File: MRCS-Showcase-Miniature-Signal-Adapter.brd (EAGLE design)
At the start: 24.5 x 24.5 mm, 19 parts

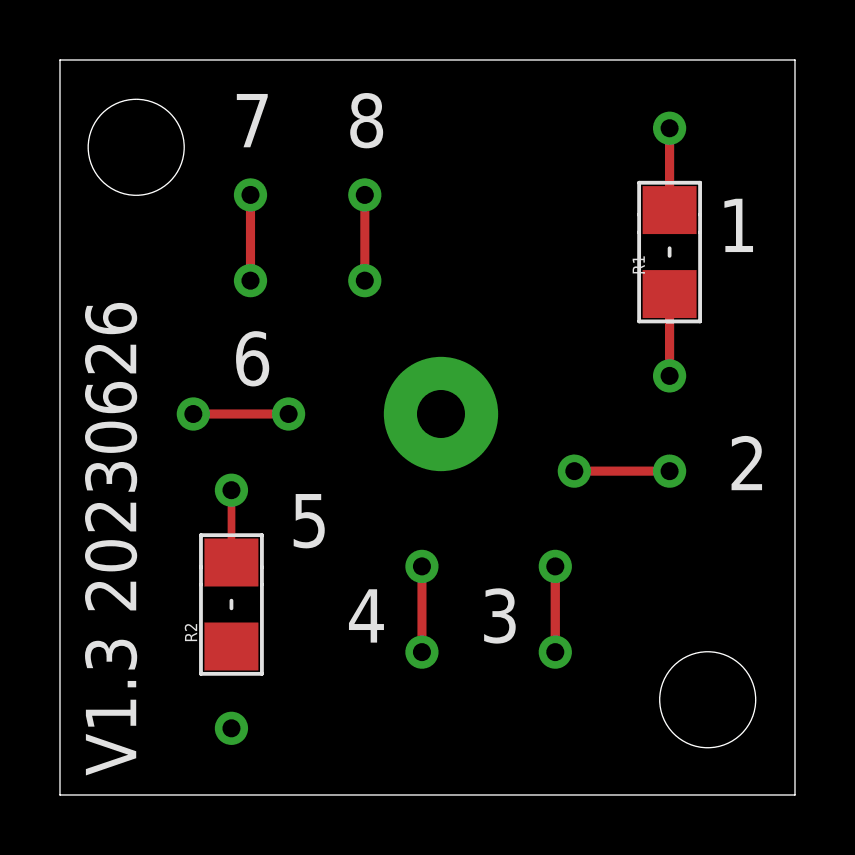
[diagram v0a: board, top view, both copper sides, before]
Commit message: First production version
Showcase miniature signal base for 1 or 2 head signal, requested by Allison Dendy
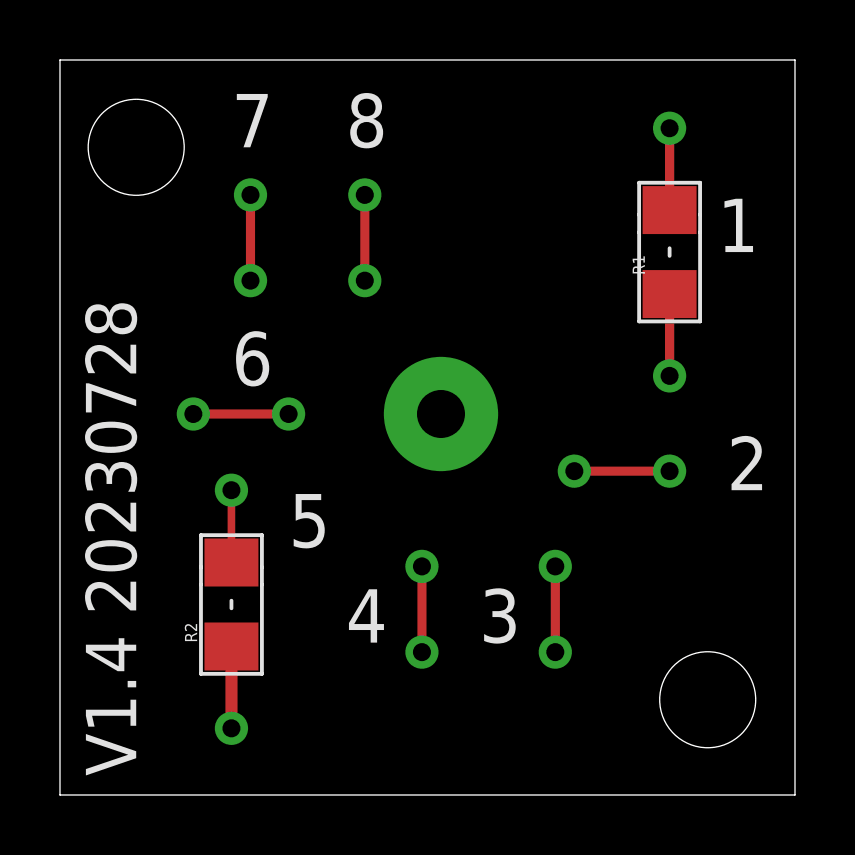
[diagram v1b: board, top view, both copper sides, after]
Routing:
- net N$3: track 0.00 -> 2.73 mm
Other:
- board text added: "R1"
- board text added: "R2"
- board text added: "V1.4 20230728"
- board text removed: "V1.3 20230626"
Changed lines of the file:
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@@
 <layer number="98" name="Guide" color="6" fill="1" visible="no" active="no"/>
 <layer number="99" name="Anatomie" color="7" fill="1" visible="no" active="no"/>
-<layer number="100" name="Muster" color="7" fill="1" visible="no" active="no"/>
-<layer number="101" name="Hidden" color="57" fill="4" visible="yes" active="yes"/>
-<layer number="102" name="Changes" color="13" fill="1" visible="yes" active="yes"/>
-<layer number="103" name="tMap" color="29" fill="4" visible="no" active="yes"/>
-<layer number="104" name="Name" color="16" fill="1" visible="yes" active="yes"/>
-<layer number="105" name="tPlate" color="7" fill="1" visible="no" active="yes"/>
-<layer number="106" name="bPlate" color="7" fill="1" visible="no" active="yes"/>
-<layer number="107" name="Crop" color="7" fill="1" visible="no" active="yes"/>
-<layer number="108" name="fp8" color="7" fill="1" visible="no" active="yes"/>
-<layer number="109" name="fp9" color="7" fill="1" visible="no" active="yes"/>
-<layer number="110" name="fp0" color="7" fill="1" visible="no" active="yes"/>
-<layer number="111" name="bdokum" color="7" fill="1" visible="no" active="yes"/>
-<layer number="112" name="tSilk" color="7" fill="1" visible="no" active="no"/>
-<layer number="113" name="IDFDebug" color="7" fill="1" visible="no" active="yes"/>
-<layer number="114" name="Rect_Pads" color="7" fill="1" visible="no" active="yes"/>
-<layer number="115" name="_tsilk" color="7" fill="1" visible="no" active="yes"/>
-<layer number="116" name="Patch_BOT" color="9" fill="4" visible="no" active="yes"/>
-<layer number="117" name="tTestmark" color="7" fill="1" visible="no" active="yes"/>
-<layer number="118" name="Rect_Pads" color="7" fill="1" visible="no" active="no"/>
-<layer number="119" name="_tNames" color="7" fill="1" visible="no" active="yes"/>
-<layer number="120" name="_bNames" color="7" fill="1" visible="no" active="yes"/>
-<layer number="121" name="_tsilk" color="7" fill="1" visible="no" active="yes"/>
-<layer number="122" name="_bsilk" color="7" fill="1" visible="no" active="yes"/>
-<layer number="123" name="tTestmark" color="7" fill="1" visible="no" active="yes"/>
-<layer number="124" name="bTestmark" color="7" fill="1" visible="no" active="yes"/>
-<layer number="125" name="_tNames" color="7" fill="1" visible="no" active="yes"/>
-<layer number="126" name="_bNames" color="7" fill="1" visible="no" active="yes"/>
-<layer number="127" name="_tValues" color="7" fill="1" visible="no" active="no"/>
-<layer number="128" name="_bValues" color="7" fill="1" visible="no" active="no"/>
-<layer number="129" name="Mask" color="7" fill="1" visible="no" active="yes"/>
-<layer number="130" name="SMDSTROOK" color="7" fill="1" visible="no" active="yes"/>
-<layer number="131" name="tAdjust" color="7" fill="1" visible="no" active="yes"/>
-<layer number="132" name="bAdjust" color="7" fill="1" visible="no" active="yes"/>
-<layer number="144" name="Drill_legend" color="7" fill="1" visible="no" active="yes"/>
-<layer number="146" name="Housing" color="7" fill="1" visible="no" active="yes"/>
-<layer number="147" name="Edge" color="7" fill="1" visible="no" active="yes"/>
-<layer number="148" name="ReferenceLC" color="7" fill="1" visible="no" active="yes"/>
-<layer number="149" name="ReferenceLS" color="7" fill="1" visible="no" active="yes"/>
-<layer number="150" name="Notes" color="7" fill="1" visible="no" active="yes"/>
-<layer number="151" name="HeatSink" color="7" fill="1" visible="no" active="yes"/>
-<layer number="152" name="_bDocu" color="7" fill="1" visible="no" active="no"/>
-<layer number="153" name="FabDoc1" color="7" fill="1" visible="no" active="yes"/>
-<layer number="154" name="FabDoc2" color="7" fill="1" visible="no" active="yes"/>
-<layer number="155" name="FabDoc3" color="7" fill="1" visible="no" active="yes"/>
-<layer number="199" name="Contour" color="7" fill="1" visible="no" active="yes"/>
-<layer number="200" name="200bmp" color="1" fill="10" visible="no" active="yes"/>
-<layer number="201" name="201bmp" color="2" fill="10" visible="no" active="yes"/>
-<layer number="202" name="202bmp" color="3" fill="10" visible="no" active="yes"/>
-<layer number="203" name="203bmp" color="4" fill="10" visible="no" active="yes"/>
-<layer number="204" name="204bmp" color="5" fill="10" visible="no" active="yes"/>
-<layer number="205" name="205bmp" color="6" fill="10" visible="no" active="yes"/>
-<layer number="206" name="206bmp" color="7" fill="10" visible="no" active="yes"/>
-<layer number="207" name="207bmp" color="8" fill="10" visible="no" active="yes"/>
-<layer number="208" name="208bmp" color="9" fill="10" visible="no" active="yes"/>
-<layer number="209" name="209bmp" color="7" fill="1" visible="no" active="yes"/>
-<layer number="210" name="210bmp" color="7" fill="1" visible="no" active="yes"/>
-<layer number="211" name="211bmp" color="12" fill="1" visible="no" active="no"/>
-<layer number="212" name="212bmp" color="13" fill="1" visible="no" active="no"/>
-<layer number="213" name="213bmp" color="14" fill="1" visible="no" active="no"/>
-<layer number="214" name="214bmp" color="15" fill="1" visible="no" active="no"/>
-<layer number="215" name="215bmp" color="16" fill="1" visible="no" active="no"/>
-<layer number="216" name="216bmp" color="17" fill="1" visible="no" active="no"/>
-<layer number="217" name="217bmp" color="18" fill="1" visible="no" active="no"/>
-<layer number="218" name="218bmp" color="19" fill="1" visible="no" active="no"/>
-<layer number="219" name="219bmp" color="20" fill="1" visible="no" active="no"/>
-<layer number="220" name="220bmp" color="21" fill="1" visible="no" active="no"/>
-<layer number="221" name="221bmp" color="22" fill="1" visible="no" active="no"/>
-<layer number="222" name="222bmp" color="23" fill="1" visible="no" active="no"/>
-<layer number="223" name="223bmp" color="24" fill="1" visible="no" active="no"/>
-<layer number="224" name="224bmp" color="25" fill="1" visible="no" active="no"/>
-<layer number="225" name="225bmp" color="7" fill="1" visible="no" active="yes"/>
-<layer number="226" name="226bmp" color="7" fill="1" visible="no" active="yes"/>
-<layer number="227" name="227bmp" color="7" fill="1" visible="no" active="yes"/>
-<layer number="228" name="228bmp" color="7" fill="1" visible="no" active="yes"/>
-<layer number="229" name="229bmp" color="7" fill="1" visible="no" active="yes"/>
-<layer number="230" name="230bmp" color="7" fill="1" visible="no" active="yes"/>
-<layer number="231" name="231bmp" color="7" fill="1" visible="no" active="yes"/>
-<layer number="232" name="Eagle3D_PG2" color="7" fill="1" visible="no" active="yes"/>
-<layer number="233" name="Eagle3D_PG3" color="7" fill="1" visible="no" active="yes"/>
-<layer number="247" name="wrappinf" color="7" fill="1" visible="no" active="yes"/>
-<layer number="248" name="Housing" color="7" fill="1" visible="no" active="no"/>
-<layer number="249" name="Edge" color="7" fill="1" visible="no" active="no"/>
-<layer number="250" name="Descript" color="3" fill="1" visible="no" active="no"/>
-<layer number="251" name="SMDround" color="12" fill="11" visible="no" active="no"/>
-<layer number="252" name="BR-BS" color="7" fill="1" visible="no" active="yes"/>
-<layer number="253" name="BR-LS" color="7" fill="1" visible="no" active="yes"/>
-<layer number="254" name="cooling" color="7" fill="1" visible="no" active="yes"/>
-<layer number="255" name="routoute" color="7" fill="1" visible="no" active="yes"/>
+<layer number="125" name="_tNames" color="14" fill="1" visible="yes" active="yes"/>
 </layers>
 <board>
@@
 <hole x="2.54" y="21.59" drill="3.2"/>
 <hole x="21.59" y="3.175" drill="3.2"/>
-<text x="2.54" y="0.635" size="1.6764" layer="21" font="vector" ratio="10" rot="R90">V1.3 20230626</text>
+<text x="2.54" y="0.635" size="1.6764" layer="21" font="vector" ratio="10" rot="R90">V1.4 20230728</text>
+<text x="19.4945" y="17.3355" size="0.4064" layer="125" font="vector" rot="R90">R1</text>
+<text x="4.572" y="5.08" size="0.4064" layer="125" font="vector" rot="R90">R2</text>
 </plain>
 <attributes>
@@
 <contactref element="R2" pad="1"/>
 <contactref element="TP2" pad="P$1"/>
-<wire x1="5.715" y1="2.2225" x2="5.715" y2="4.95" width="0" layer="19" extent="1-1"/>
+<wire x1="5.715" y1="2.2225" x2="5.715" y2="4.95" width="0.4064" layer="1"/>
 </signal>
 <signal name="N$4">
